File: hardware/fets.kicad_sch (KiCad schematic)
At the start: 21 parts, among them Q701 CMSA30N06T, Q702 CMSA30N06T, Q703 CMSA30N06T

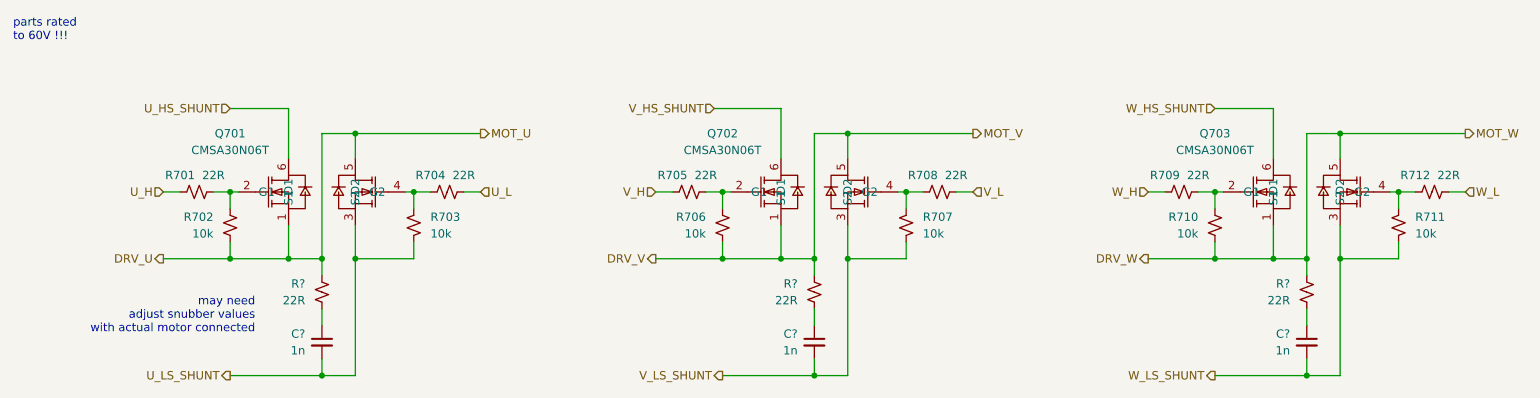
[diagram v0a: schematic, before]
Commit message: finish component selection
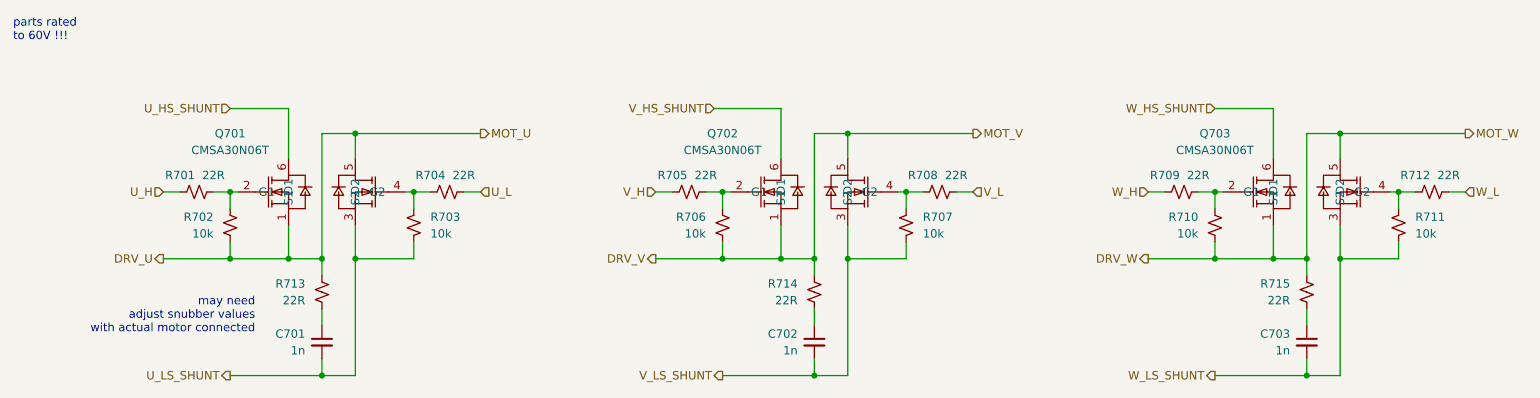
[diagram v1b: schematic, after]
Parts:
- gave numbers to parts that had none: 6
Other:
- company: (none) -> matei repair lab
- title: (none) -> POWER STAGE
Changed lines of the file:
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@@
 (kicad_sch (version 20230121) (generator eeschema)
   (paper "A4")
+  (title_block
+    (title "POWER STAGE")
+    (date "2023-10-11")
+    (rev "0.1")
+    (company "matei repair lab")
+  )
   (junction (at 224.79 90.17) (diameter 0) (color 0 0 0 0)
   )
@@
     (pin "2")
     (instances
-      (project "sfoc-stepper"
+      (project "lemon-pepper"
         (path "/0306e2fa-4433-4288-91d9-65a3484207ad/4ae515ef-7634-40dd-8c26-7b515d9d6b82"
           (reference "R704") (unit 1)
@@
     (pin "2")
     (instances
-      (project "sfoc-stepper"
+      (project "lemon-pepper"
         (path "/0306e2fa-4433-4288-91d9-65a3484207ad/4ae515ef-7634-40dd-8c26-7b515d9d6b82"
           (reference "R710") (unit 1)
@@
   (symbol (lib_id "Device:C_Small") (at 80.01 102.87 0) (unit 1)
     (in_bom yes) (on_board yes) (dnp no)
-    (property "Reference" "C?" (at 77.47 101.6063 0)
+    (property "Reference" "C701" (at 77.47 101.6063 0)
       (effects (font (size 1.27 1.27)) (justify right))
     )
@@
     (pin "2")
     (instances
-      (project "sfoc-stepper"
+      (project "lemon-pepper"
         (path "/0306e2fa-4433-4288-91d9-65a3484207ad/4ae515ef-7634-40dd-8c26-7b515d9d6b82"
-          (reference "C?") (unit 1)
+          (reference "C701") (unit 1)
         )
       )
@@
     (pin "2")
     (instances
-      (project "sfoc-stepper"
+      (project "lemon-pepper"
         (path "/0306e2fa-4433-4288-91d9-65a3484207ad/4ae515ef-7634-40dd-8c26-7b515d9d6b82"
           (reference "R708") (unit 1)
@@
     (pin "2")
     (instances
-      (project "sfoc-stepper"
+      (project "lemon-pepper"
         (path "/0306e2fa-4433-4288-91d9-65a3484207ad/4ae515ef-7634-40dd-8c26-7b515d9d6b82"
           (reference "R706") (unit 1)
@@
     (pin "2")
     (instances
-      (project "sfoc-stepper"
+      (project "lemon-pepper"
         (path "/0306e2fa-4433-4288-91d9-65a3484207ad/4ae515ef-7634-40dd-8c26-7b515d9d6b82"
           (reference "R711") (unit 1)
@@
   (symbol (lib_id "Device:C_Small") (at 229.87 102.87 0) (unit 1)
     (in_bom yes) (on_board yes) (dnp no)
-    (property "Reference" "C?" (at 227.33 101.6063 0)
+    (property "Reference" "C703" (at 227.33 101.6063 0)
       (effects (font (size 1.27 1.27)) (justify right))
     )
@@
     (pin "2")
     (instances
-      (project "sfoc-stepper"
+      (project "lemon-pepper"
         (path "/0306e2fa-4433-4288-91d9-65a3484207ad/4ae515ef-7634-40dd-8c26-7b515d9d6b82"
-          (reference "C?") (unit 1)
+          (reference "C703") (unit 1)
         )
       )
@@
     (pin "2")
     (instances
-      (project "sfoc-stepper"
+      (project "lemon-pepper"
         (path "/0306e2fa-4433-4288-91d9-65a3484207ad/4ae515ef-7634-40dd-8c26-7b515d9d6b82"
           (reference "R702") (unit 1)
@@
     (pin "2")
     (instances
-      (project "sfoc-stepper"
+      (project "lemon-pepper"
         (path "/0306e2fa-4433-4288-91d9-65a3484207ad/4ae515ef-7634-40dd-8c26-7b515d9d6b82"
           (reference "R703") (unit 1)
@@
     (pin "6")
     (instances
-      (project "sfoc-stepper"
+      (project "lemon-pepper"
         (path "/0306e2fa-4433-4288-91d9-65a3484207ad/4ae515ef-7634-40dd-8c26-7b515d9d6b82"
           (reference "Q701") (unit 1)
@@
     (pin "6")
     (instances
-      (project "sfoc-stepper"
+      (project "lemon-pepper"
         (path "/0306e2fa-4433-4288-91d9-65a3484207ad/4ae515ef-7634-40dd-8c26-7b515d9d6b82"
           (reference "Q703") (unit 1)
@@
   (symbol (lib_id "Device:C_Small") (at 154.94 102.87 0) (unit 1)
     (in_bom yes) (on_board yes) (dnp no)
-    (property "Reference" "C?" (at 152.4 101.6063 0)
+    (property "Reference" "C702" (at 152.4 101.6063 0)
       (effects (font (size 1.27 1.27)) (justify right))
     )
@@
     (pin "2")
     (instances
-      (project "sfoc-stepper"
+      (project "lemon-pepper"
         (path "/0306e2fa-4433-4288-91d9-65a3484207ad/4ae515ef-7634-40dd-8c26-7b515d9d6b82"
-          (reference "C?") (unit 1)
+          (reference "C702") (unit 1)
         )
       )
@@
   (symbol (lib_id "Device:R_Small_US") (at 80.01 95.25 0) (unit 1)
     (in_bom yes) (on_board yes) (dnp no)
-    (property "Reference" "R?" (at 77.47 93.98 0)
+    (property "Reference" "R713" (at 77.47 93.98 0)
       (effects (font (size 1.27 1.27)) (justify right))
     )
@@
     (pin "2")
     (instances
-      (project "sfoc-stepper"
+      (project "lemon-pepper"
         (path "/0306e2fa-4433-4288-91d9-65a3484207ad/4ae515ef-7634-40dd-8c26-7b515d9d6b82"
-          (reference "R?") (unit 1)
+          (reference "R713") (unit 1)
         )
       )
@@
     (pin "2")
     (instances
-      (project "sfoc-stepper"
+      (project "lemon-pepper"
         (path "/0306e2fa-4433-4288-91d9-65a3484207ad/4ae515ef-7634-40dd-8c26-7b515d9d6b82"
           (reference "R705") (unit 1)
@@
     (pin "2")
     (instances
-      (project "sfoc-stepper"
+      (project "lemon-pepper"
         (path "/0306e2fa-4433-4288-91d9-65a3484207ad/4ae515ef-7634-40dd-8c26-7b515d9d6b82"
           (reference "R707") (unit 1)
@@
     (pin "2")
     (instances
-      (project "sfoc-stepper"
+      (project "lemon-pepper"
         (path "/0306e2fa-4433-4288-91d9-65a3484207ad/4ae515ef-7634-40dd-8c26-7b515d9d6b82"
           (reference "R709") (unit 1)
@@
   (symbol (lib_id "Device:R_Small_US") (at 154.94 95.25 0) (unit 1)
     (in_bom yes) (on_board yes) (dnp no)
-    (property "Reference" "R?" (at 152.4 93.98 0)
+    (property "Reference" "R714" (at 152.4 93.98 0)
       (effects (font (size 1.27 1.27)) (justify right))
     )
@@
     (pin "2")
     (instances
-      (project "sfoc-stepper"
+      (project "lemon-pepper"
         (path "/0306e2fa-4433-4288-91d9-65a3484207ad/4ae515ef-7634-40dd-8c26-7b515d9d6b82"
-          (reference "R?") (unit 1)
+          (reference "R714") (unit 1)
         )
       )
@@
     (pin "6")
     (instances
-      (project "sfoc-stepper"
+      (project "lemon-pepper"
         (path "/0306e2fa-4433-4288-91d9-65a3484207ad/4ae515ef-7634-40dd-8c26-7b515d9d6b82"
           (reference "Q702") (unit 1)
@@
     (pin "2")
     (instances
-      (project "sfoc-stepper"
+      (project "lemon-pepper"
         (path "/0306e2fa-4433-4288-91d9-65a3484207ad/4ae515ef-7634-40dd-8c26-7b515d9d6b82"
           (reference "R712") (unit 1)
@@
   (symbol (lib_id "Device:R_Small_US") (at 229.87 95.25 0) (unit 1)
     (in_bom yes) (on_board yes) (dnp no)
-    (property "Reference" "R?" (at 227.33 93.98 0)
+    (property "Reference" "R715" (at 227.33 93.98 0)
       (effects (font (size 1.27 1.27)) (justify right))
     )
@@
     (pin "2")
     (instances
-      (project "sfoc-stepper"
+      (project "lemon-pepper"
         (path "/0306e2fa-4433-4288-91d9-65a3484207ad/4ae515ef-7634-40dd-8c26-7b515d9d6b82"
-          (reference "R?") (unit 1)
+          (reference "R715") (unit 1)
         )
       )
@@
     (pin "2")
     (instances
-      (project "sfoc-stepper"
+      (project "lemon-pepper"
         (path "/0306e2fa-4433-4288-91d9-65a3484207ad/4ae515ef-7634-40dd-8c26-7b515d9d6b82"
           (reference "R701") (unit 1)
